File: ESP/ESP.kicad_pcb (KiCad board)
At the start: 4 copper layers, 33.7 x 17.8 mm, 28 parts, among them J3 USB_B_Micro, J4 Micro_SD_Card_Det, Q1 mmbt2222, Q2 mmbt2222, U1 ESP32-PICO-D4, U2 AP2112K-3.3, U3 CP2104

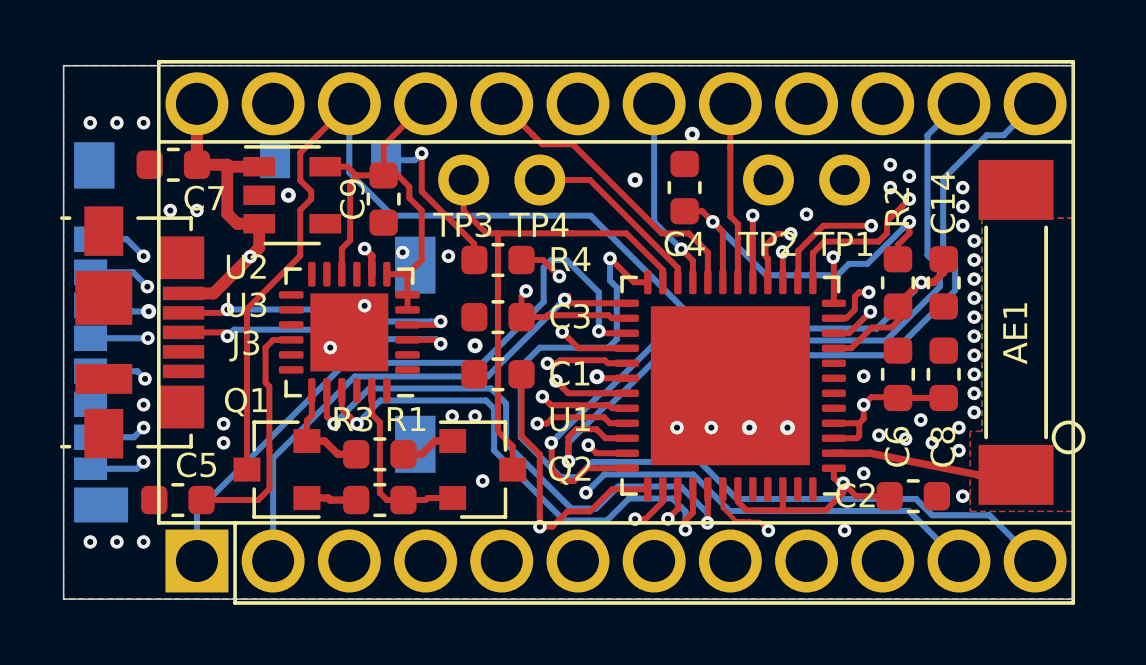
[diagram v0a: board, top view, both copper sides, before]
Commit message: changed VCC of CP2104
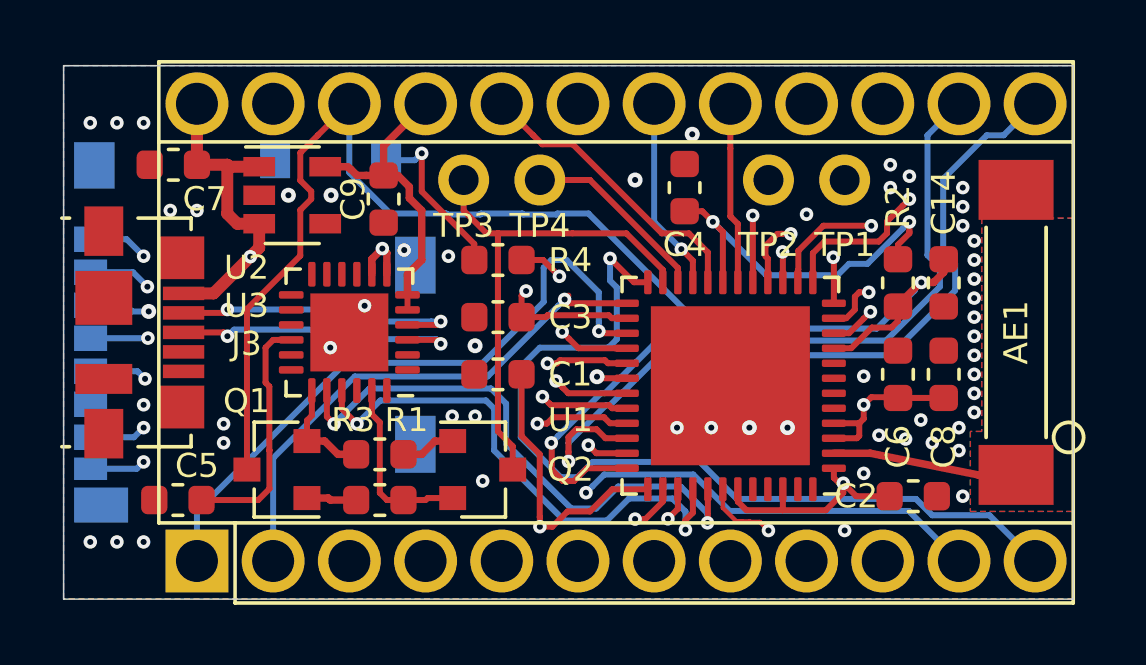
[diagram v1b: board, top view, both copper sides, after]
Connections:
- U3 pad 10: +3V3 -> Net-(U3-Pad10)
- U3 pad 7: +3V3 -> +5V
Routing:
- net +3V3: track 83.6 -> 79.4 mm
- net +5V: track 15.8 -> 17.4 mm
- net GND: vias 53 -> 54

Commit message: blindly dumped everything
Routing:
- net Net-(J4-Pad10): track 5.56 -> 5.00 mm
- net GND: vias 54 -> 55
